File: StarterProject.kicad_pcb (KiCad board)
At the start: 2 copper layers, 95 x 75 mm, 54 parts, among them J1 POWER_MINION, J10 EX_HDLT, J11 EX_BRAKELIGHT, J12 +12V, J13 GND, J14 POWER_LEADERBOARD, J15 F/R, J16 TURN_SIGNAL, J17 NEU_INDICATOR, J18 FOR_INDICATOR, J19 REV_INDICATOR, J2 CRUISE_SET, J20 CRUZ_SET, J21 CRUZ_EN, J22 REGEN, J3 CRUISE_ENABLE, J4 REGEN, J5 HZD, J6 EX_RIGHTBLINK, J7 EX_LEFTBLINK, J8 IN_RIGHTBLINK, J9 IN_LEFTBLINK, SW1 CRUISE_SET_SW, SW2 CRUISE_ENABLE_SW, SW3 REGEN_SW, SW4 HZD_SW, SW5 F/R, SW6 TURN_SIGNAL_SW

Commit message: Updated PCB
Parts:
- added H1: MountingHole, MountingHole:MountingHole_3mm_Pad, F.Cu at (125.0, 32.5)
- added H2: MountingHole, MountingHole:MountingHole_3mm_Pad, F.Cu at (35.0, 32.5)
- added H3: MountingHole, MountingHole:MountingHole_3mm_Pad, F.Cu at (35.0, 107.5)
- added H4: MountingHole, MountingHole:MountingHole_3mm_Pad, F.Cu at (125.0, 107.5)
- moved LOGO1 45.3 mm to (104.0, 54.5)
- moved J13 9.57 mm to (58.1, 53.5)
- moved J14 9.57 mm to (45.2, 55.0)
- moved J1 8.41 mm to (45.0, 40.0)
- moved J12 8.41 mm to (57.9, 38.6)
- moved J15 4.74 mm to (39.2, 96.3)
- moved SW5 4.74 mm to (54.5, 95.0)
- moved J16 4.35 mm to (39.0, 76.3)
- moved SW6 4.35 mm to (54.5, 76.4)
- moved J2 4.19 mm to (75.2, 103.0)
- moved J3 4.19 mm to (75.2, 90.2)
- moved J4 4.19 mm to (75.2, 77.3)
- moved J5 4.19 mm to (75.2, 64.8)
- moved SW1 4.19 mm to (65.4, 106.6)
- moved SW2 4.19 mm to (65.4, 93.7)
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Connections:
- net Net-(J1-Pad2) renamed GND
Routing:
- net GND: track 32.3 -> 0.00 mm
- net Net-(D1-Pad1): track 38.9 -> 42.1 mm
- net Net-(D2-Pad2): track 27.5 -> 30.4 mm
- net Net-(D1-Pad2): track 29.9 -> 32.4 mm
- net Net-(D10-Pad1): track 17.3 -> 19.7 mm
- net Net-(D2-Pad1): track 29.7 -> 32.0 mm
- net Net-(J20-Pad1): track 7.14 -> 5.06 mm
- net Net-(D12-Pad1): track 11.2 -> 9.15 mm
- net Net-(D5-Pad2): track 18.8 -> 20.6 mm
- net Net-(D6-Pad2): track 28.7 -> 30.3 mm
- net Net-(D5-Pad1): track 20.3 -> 21.9 mm
- net Net-(D6-Pad1): track 41.0 -> 42.1 mm
- net Net-(D11-Pad1): track 11.5 -> 12.2 mm
- net Net-(J1-Pad1): track 32.3 -> 31.7 mm
- added copper zone on B.Cu, net GND
- added copper zone on F.Cu, net GND
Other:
- board size 95 x 75 mm -> 99 x 86 mm
- board text added: "UTSVT- Controls Minion Test v0.1 Pratyush Patra"

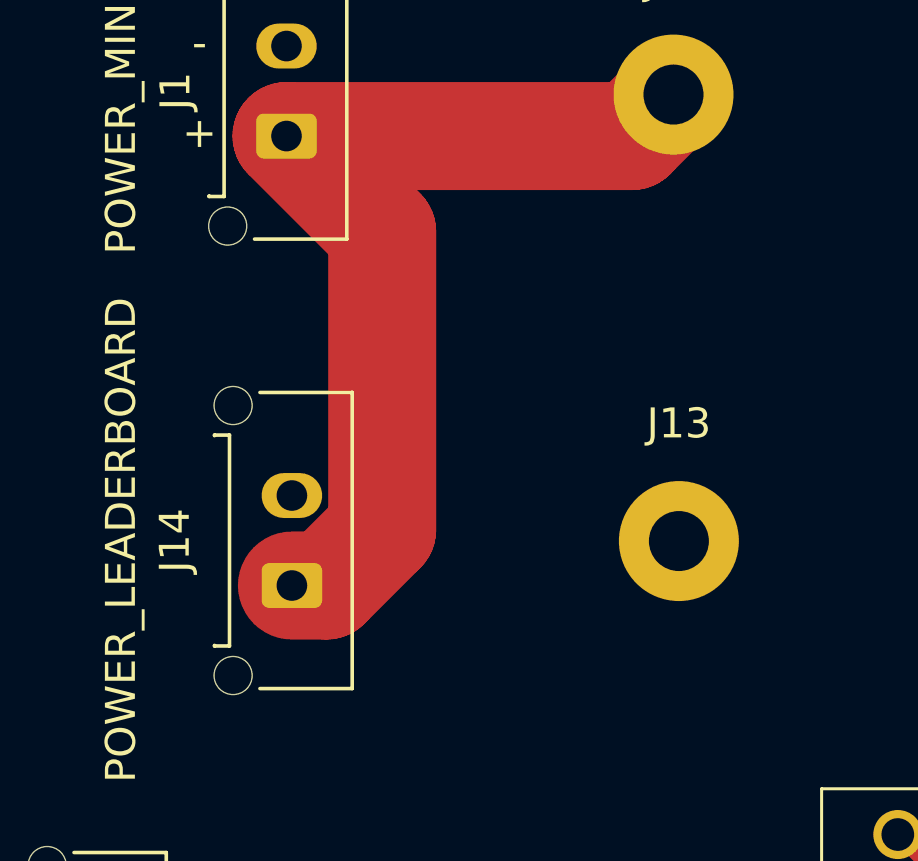
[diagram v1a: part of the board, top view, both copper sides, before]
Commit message: Labelling Update
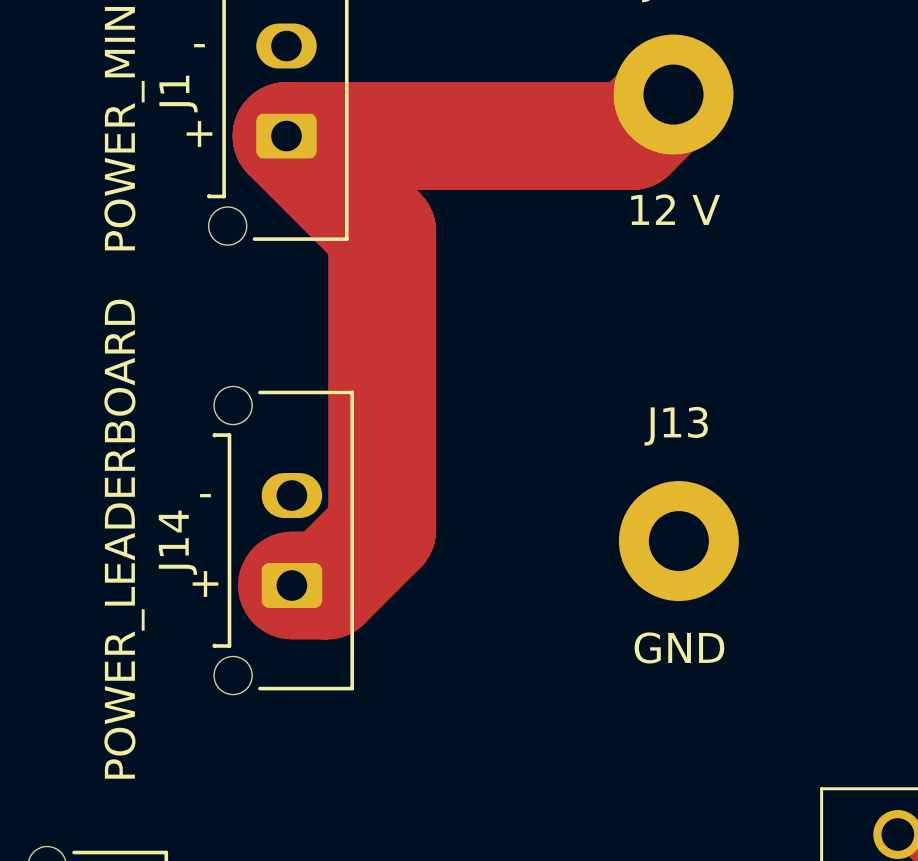
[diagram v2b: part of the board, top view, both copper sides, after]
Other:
- board text added: "12 V"
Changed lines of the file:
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@@
     )
     (pad_to_mask_clearance 0)
-    (grid_origin 54.5 53.5)
+    (grid_origin 57.7 30.5)
     (pcbplotparams
       (layerselection 0x00010fc_ffffffff)
@@
       (effects (font (size 1 1) (thickness 0.15)))
     )
-    (fp_text value "GND" (at 0 -0.5) (layer "F.Fab")
+    (fp_text value "GND" (at -0.02 -3.6) (layer "F.SilkS")
       (effects (font (size 1 1) (thickness 0.15)))
     )
@@
     (effects (font (size 1 1) (thickness 0.15)))
   )
+  (gr_text "-\n" (at 42.3 51.9) (layer "F.SilkS")
+    (effects (font (size 1 1) (thickness 0.15)))
+  )
   (gr_text "-\n" (at 42.1 36.9) (layer "F.SilkS")
     (effects (font (size 1 1) (thickness 0.15)))
@@
     (effects (font (size 1 1) (thickness 0.15)))
   )
+  (gr_text "+" (at 42.3 54.9) (layer "F.SilkS")
+    (effects (font (size 1 1) (thickness 0.15)))
+  )
   (gr_text "-\n" (at 113 41.75) (layer "F.SilkS")
     (effects (font (size 1 1) (thickness 0.15)))
@@
     (effects (font (size 1 1) (thickness 0.15)))
   )
+  (gr_text "12 V" (at 57.9 42.5) (layer "F.SilkS")
+    (effects (font (size 1 1) (thickness 0.15)))
+  )
   (gr_text "-\n" (at 104.202 96.469 180) (layer "F.SilkS")
     (effects (font (size 1 1) (thickness 0.15)))
@@
     )
   )
+  (group "" (id 751ef0fe-e673-4d0e-84c9-618efa213584)
+    (members
+      15717514-037f-44f4-a42e-d4ab5486dca5
+      82e83c89-13c0-4e14-9615-bd18f2360f7f
+    )
+  )
